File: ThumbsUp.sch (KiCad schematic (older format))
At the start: 120 parts, among them J1 Conn_01x04_Male, J10 Raiser_Male, J11 Raiser_Female, J12 Raiser_Male, J13 Raiser_Female, J14 Raiser_Male, J15 Raiser_Female, J16 Raiser_Male, J17 Raiser_Female, J18 Raiser_Male, J19 52559-1233, J2 Conn_01x04_Male, J20 Conn_01x04_Female, J21 Conn_01x04_Female, J22 Conn_01x04_Female, J23 Conn_01x04_Female, J24 Conn_01x04_Male, J25 Conn_01x04_Male, J26 Conn_01x04_Male, J27 Conn_01x04_Male, J28 Conn_01x04_Female, J29 Conn_01x04_Female, J3 Conn_01x04_Female, J30 Conn_01x04_Female, J31 Conn_01x04_Female, J4 Conn_01x04_Male, J5 Conn_01x04_Female, J6 Conn_01x04_Male, J7 Conn_01x04_Male, J8 Conn_01x04_Male, J9 Raiser_Female, U1 ProMicro

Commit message: WIP
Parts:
- added SW1: SW_Push, random-keyboard-parts:SKQG-1155865, symbol Switch:SW_Push
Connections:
- net COL0: now also U1.14 (B2)
- net COL1: now also U1.13 (B6)
- net COL2: now also U1.12 (B5)
- net COL3: now also U1.11 (B4)
- net COL4: now also U1.10 (E6)
- net COL5: now also U1.9 (D7)
- net COL6: now also U1.15 (B3)
- net COL7: now also U1.20 (F4)
- net COL8: now also U1.19 (F5)
- net COL9: now also U1.18 (F6)
- net COLA: now also U1.17 (F7)
- net COLB: now also U1.16 (B1)
- net GND: now also U1.23 (GND), SW1.2
- net ROW0: now also U1.1 (TX)
- net ROW1: now also U1.2 (RX)
- net ROW2: now also U1.7 (D4)
- net ROW3: now also U1.8 (C6)
- net SCL: now also U1.6 (SCL)
- net SDA: now also U1.5 (SDA)
- net VCC: now also U1.21 (VCC)
- net RST: now reaches U1.22 (RST)
- net RST: now also SW1.1
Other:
- moved on the sheet: U1
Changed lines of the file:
@@
 GND-TOP
 NoConn ~ 9300 2750
+Text GLabel 3400 3550 0    50   Input ~ 0
+SDA
+Text GLabel 3400 3650 0    50   Input ~ 0
+SCL
+Text GLabel 3400 3150 0    50   Input ~ 0
+ROW0
+Text GLabel 3400 3250 0    50   Input ~ 0
+ROW1
+Text GLabel 3400 3750 0    50   Input ~ 0
+ROW2
+Text GLabel 3400 3850 0    50   Input ~ 0
+ROW3
+Text GLabel 3400 3950 0    50   Input ~ 0
+COL5
+Text GLabel 3400 4050 0    50   Input ~ 0
+COL4
+Text GLabel 3400 4150 0    50   Input ~ 0
+COL3
+Text GLabel 3400 4250 0    50   Input ~ 0
+COL2
+Text GLabel 4800 4250 2    50   Input ~ 0
+COL1
 $Comp
 L promicro:ProMicro U1
 U 1 1 63784203
-P 3350 3650
-F 0 "U1" H 3350 4687 60  0000 C CNN
-F 1 "ProMicro" H 3350 4581 60  0000 C CNN
-F 2 "promicro:ProMicro" H 3450 2600 60  0001 C CNN
-F 3 "" H 3450 2600 60  0000 C CNN
-	1    3350 3650
+P 4100 3900
+F 0 "U1" H 4100 4937 60  0000 C CNN
+F 1 "ProMicro" H 4100 4831 60  0000 C CNN
+F 2 "promicro:ProMicro" H 4200 2850 60  0001 C CNN
+F 3 "" H 4200 2850 60  0000 C CNN
+	1    4100 3900
 	1    0    0    -1
 $EndComp
+Text GLabel 4800 4150 2    50   Input ~ 0
+COL0
+Text GLabel 4800 4050 2    50   Input ~ 0
+COL6
+Text GLabel 4800 3950 2    50   Input ~ 0
+COLB
+Text GLabel 4800 3850 2    50   Input ~ 0
+COLA
+Text GLabel 4800 3750 2    50   Input ~ 0
+COL9
+Text GLabel 4800 3650 2    50   Input ~ 0
+COL8
+Text GLabel 4800 3550 2    50   Input ~ 0
+COL7
+$Comp
+L power:VCC #PWR0101
+U 1 1 63813373
+P 4800 3450
+F 0 "#PWR0101" H 4800 3300 50  0001 C CNN
+F 1 "VCC" V 4817 3578 50  0000 L CNN
+F 2 "" H 4800 3450 50  0001 C CNN
+F 3 "" H 4800 3450 50  0001 C CNN
+	1    4800 3450
+	0    1    1    0
+$EndComp
+$Comp
+L power:GND #PWR0102
+U 1 1 63814A0B
+P 5200 3250
+F 0 "#PWR0102" H 5200 3000 50  0001 C CNN
+F 1 "GND" H 5205 3077 50  0000 C CNN
+F 2 "" H 5200 3250 50  0001 C CNN
+F 3 "" H 5200 3250 50  0001 C CNN
+	1    5200 3250
+	1    0    0    -1
+$EndComp
+Wire Wire Line
+	4800 3250 5200 3250
+Text GLabel 4800 3350 2    50   Input ~ 0
+RST
+$Comp
+L Switch:SW_Push SW1
+U 1 1 63887BED
+P 4050 5000
+F 0 "SW1" H 4050 5285 50  0000 C CNN
+F 1 "SW_Push" H 4050 5194 50  0000 C CNN
+F 2 "random-keyboard-parts:SKQG-1155865" H 4050 5200 50  0001 C CNN
+F 3 "~" H 4050 5200 50  0001 C CNN
+	1    4050 5000
+	1    0    0    -1
+$EndComp
+Text GLabel 3850 5000 0    50   Input ~ 0
+RST
+$Comp
+L power:GND #PWR0104
+U 1 1 6388A683
+P 4250 5000
+F 0 "#PWR0104" H 4250 4750 50  0001 C CNN
+F 1 "GND" H 4255 4827 50  0000 C CNN
+F 2 "" H 4250 5000 50  0001 C CNN
+F 3 "" H 4250 5000 50  0001 C CNN
+	1    4250 5000
+	1    0    0    -1
+$EndComp

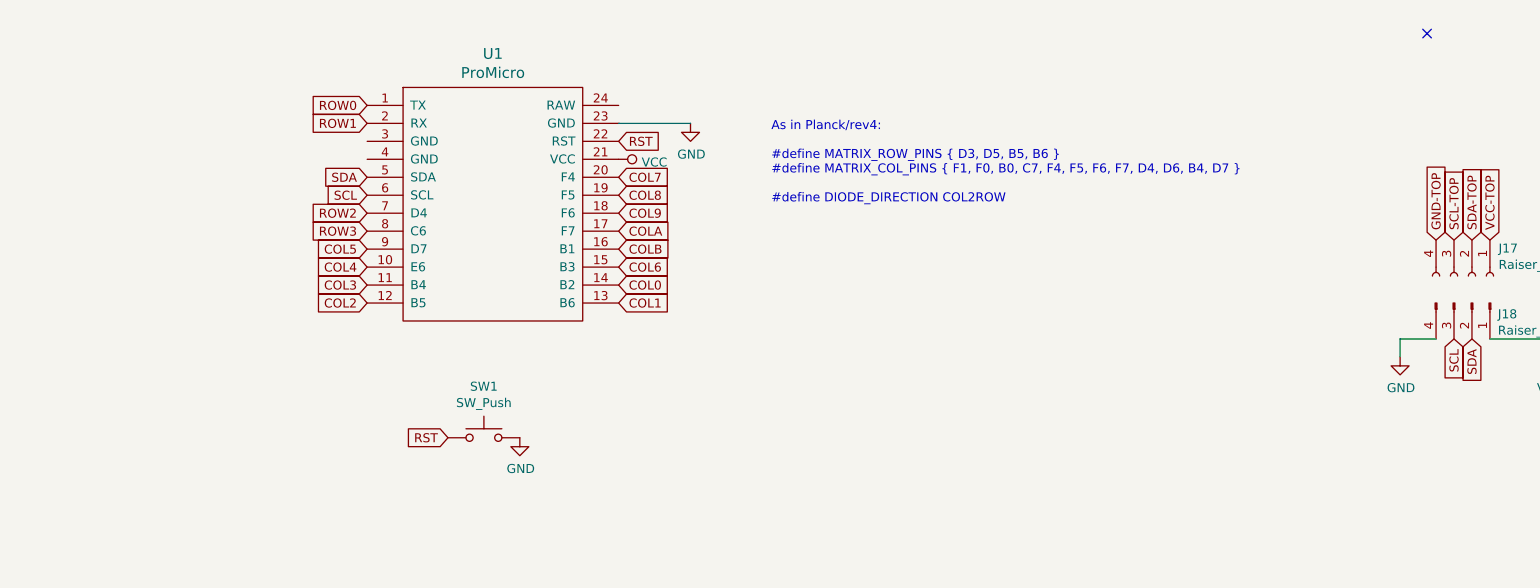
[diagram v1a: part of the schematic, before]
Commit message: Added power connector, pullup resistors for the trackpad, made the promicro holes bigger to fit the sockets.
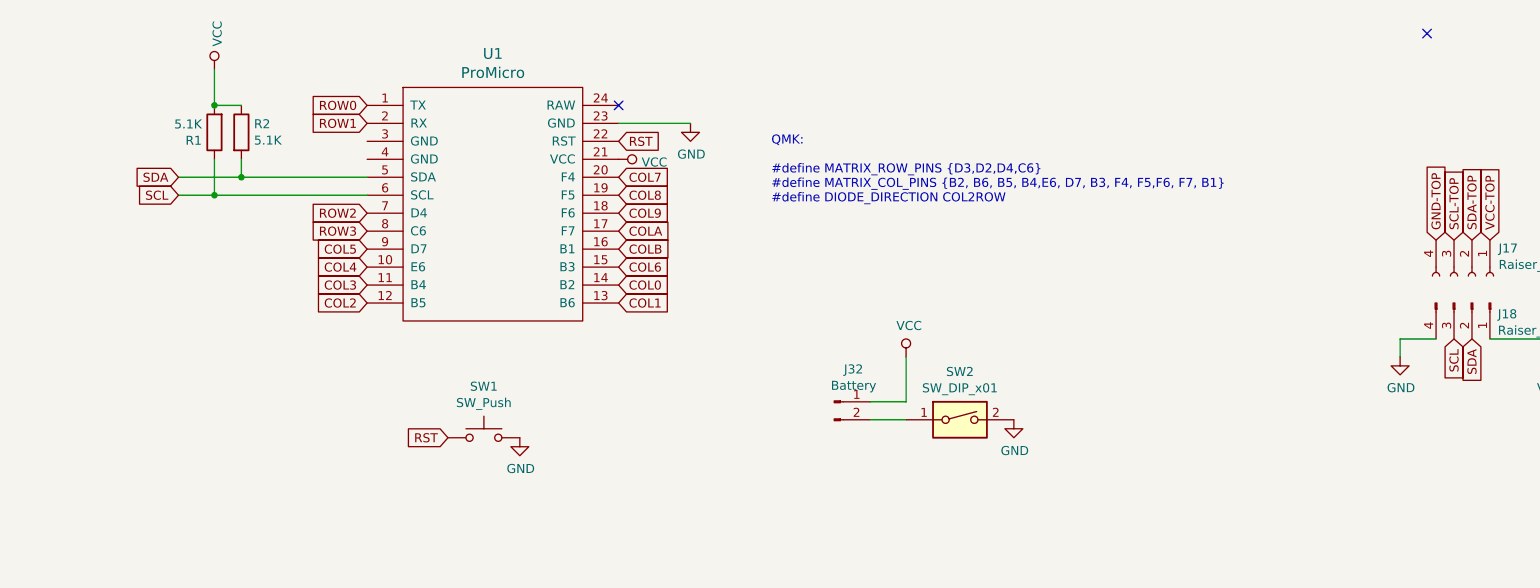
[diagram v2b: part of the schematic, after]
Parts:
- added J32: Battery, Connector_PinHeader_2.54mm:PinHeader_1x02_P2.54mm_Vertical, symbol Connector:Conn_01x02_Male
- added R1, R2: 5.1K, Resistor_SMD:R_0805_2012Metric, symbol Device:R
- added SW2: SW_DIP_x01, 1825232-1:18252321, symbol Switch:SW_DIP_x01
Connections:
- net GND: now also SW2.2
- net SCL: now also R1.1
- net SDA: now also R2.2
- net VCC: now also J32.1 (Pin_1), R1.2, R2.1
- new net: J32.2 (Pin_2), SW2.1
- no-connect marks 46 -> 47
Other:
- note added: "QMK: \n\n#define MATRIX_ROW_PINS {D3,D2,D4,C6}\n#define MATRIX_COL_PINS {B2, B6, B5, B4,E6, D7, B3, F4, F5,F6, F7, B1}\n#define DIODE_DIRECTION COL2ROW\n"
- note removed: "As in Planck/rev4:\n\n#define MATRIX_ROW_PINS { D3, D5, B5, B6 }\n#define MATRIX_COL_PINS { F1, F0, B0, C7, F4, F5, F6, F7, D4, D6, B4, D7 }\n\n#define DIODE_DIRECTION COL2ROW\n"
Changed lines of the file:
@@
 	10000 8750 10000 9900
 Text Notes 5650 3700 0    50   ~ 0
-As in Planck/rev4:\n\n#define MATRIX_ROW_PINS { D3, D5, B5, B6 }\n#define MATRIX_COL_PINS { F1, F0, B0, C7, F4, F5, F6, F7, D4, D6, B4, D7 }\n\n#define DIODE_DIRECTION COL2ROW\n
+QMK: \n\n#define MATRIX_ROW_PINS {D3,D2,D4,C6}\n#define MATRIX_COL_PINS {B2, B6, B5, B4,E6, D7, B3, F4, F5,F6, F7, B1}\n#define DIODE_DIRECTION COL2ROW\n
 $Comp
 L Connector:Conn_01x04_Female J11
@@
 GND-TOP
 NoConn ~ 9300 2750
-Text GLabel 3400 3550 0    50   Input ~ 0
+Text GLabel 2350 3550 0    50   Input ~ 0
 SDA
-Text GLabel 3400 3650 0    50   Input ~ 0
+Text GLabel 2350 3650 0    50   Input ~ 0
 SCL
 Text GLabel 3400 3150 0    50   Input ~ 0
@@
 	1    0    0    -1
 $EndComp
+Wire Wire Line
+	2350 3550 2700 3550
+Wire Wire Line
+	2350 3650 2550 3650
+$Comp
+L Device:R R2
+U 1 1 63B2EE4B
+P 2700 3300
+F 0 "R2" H 2770 3346 50  0000 L CNN
+F 1 "5.1K" H 2770 3255 50  0000 L CNN
+F 2 "Resistor_SMD:R_0805_2012Metric" V 2630 3300 50  0001 C CNN
+F 3 "~" H 2700 3300 50  0001 C CNN
+	1    2700 3300
+	1    0    0    -1
+$EndComp
+$Comp
+L Device:R R1
+U 1 1 63B2CC84
+P 2550 3300
+F 0 "R1" H 2620 3346 50  0000 L CNN
+F 1 "5.1K" H 2620 3255 50  0000 L CNN
+F 2 "Resistor_SMD:R_0805_2012Metric" V 2480 3300 50  0001 C CNN
+F 3 "~" H 2550 3300 50  0001 C CNN
+	1    2550 3300
+	-1   0    0    1
+$EndComp
+Wire Wire Line
+	2550 3450 2550 3650
+Connection ~ 2550 3650
+Wire Wire Line
+	2550 3650 3400 3650
+Wire Wire Line
+	2700 3450 2700 3550
+Connection ~ 2700 3550
+Wire Wire Line
+	2700 3550 3400 3550
+$Comp
+L power:VCC #PWR0106
+U 1 1 63BE00E5
+P 2550 2950
+F 0 "#PWR0106" H 2550 2800 50  0001 C CNN
+F 1 "VCC" V 2567 3078 50  0000 L CNN
+F 2 "" H 2550 2950 50  0001 C CNN
+F 3 "" H 2550 2950 50  0001 C CNN
+	1    2550 2950
+	1    0    0    -1
+$EndComp
+Wire Wire Line
+	2550 3150 2550 2950
+Wire Wire Line
+	2700 3150 2550 3150
+Connection ~ 2550 3150
+$Comp
+L Connector:Conn_01x02_Male J32
+U 1 1 63C60EFF
+P 6000 4800
+F 0 "J32" H 6108 4981 50  0000 C CNN
+F 1 "Battery" H 6108 4890 50  0000 C CNN
+F 2 "Connector_PinHeader_2.54mm:PinHeader_1x02_P2.54mm_Vertical" H 6000 4800 50  0001 C CNN
+F 3 "~" H 6000 4800 50  0001 C CNN
+	1    6000 4800
+	1    0    0    -1
+$EndComp
+$Comp
+L Switch:SW_DIP_x01 SW2
+U 1 1 63C62925
+P 6700 4900
+F 0 "SW2" H 6700 5167 50  0000 C CNN
+F 1 "SW_DIP_x01" H 6700 5076 50  0000 C CNN
+F 2 "1825232-1:18252321" H 6700 4900 50  0001 C CNN
+F 3 "~" H 6700 4900 50  0001 C CNN
+	1    6700 4900
+	1    0    0    -1
+$EndComp
+$Comp
+L power:VCC #PWR0107
+U 1 1 63C63335
+P 6400 4550
+F 0 "#PWR0107" H 6400 4400 50  0001 C CNN
+F 1 "VCC" H 6417 4723 50  0000 C CNN
+F 2 "" H 6400 4550 50  0001 C CNN
+F 3 "" H 6400 4550 50  0001 C CNN
+	1    6400 4550
+	1    0    0    -1
+$EndComp
+Wire Wire Line
+	6200 4800 6400 4800
+Wire Wire Line
+	6400 4800 6400 4550
+Wire Wire Line
+	6200 4900 6400 4900
+$Comp
+L power:GND #PWR0108
+U 1 1 63CAF318
+P 7000 4900
+F 0 "#PWR0108" H 7000 4650 50  0001 C CNN
+F 1 "GND" H 7005 4727 50  0000 C CNN
+F 2 "" H 7000 4900 50  0001 C CNN
+F 3 "" H 7000 4900 50  0001 C CNN
+	1    7000 4900
+	1    0    0    -1
+$EndComp
+NoConn ~ 4800 3150
 $EndSCHEMATC
